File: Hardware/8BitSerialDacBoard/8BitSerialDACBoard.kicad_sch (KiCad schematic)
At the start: 28 parts, among them J1 Conn_01x08, U1 SN74LV595APWRG4

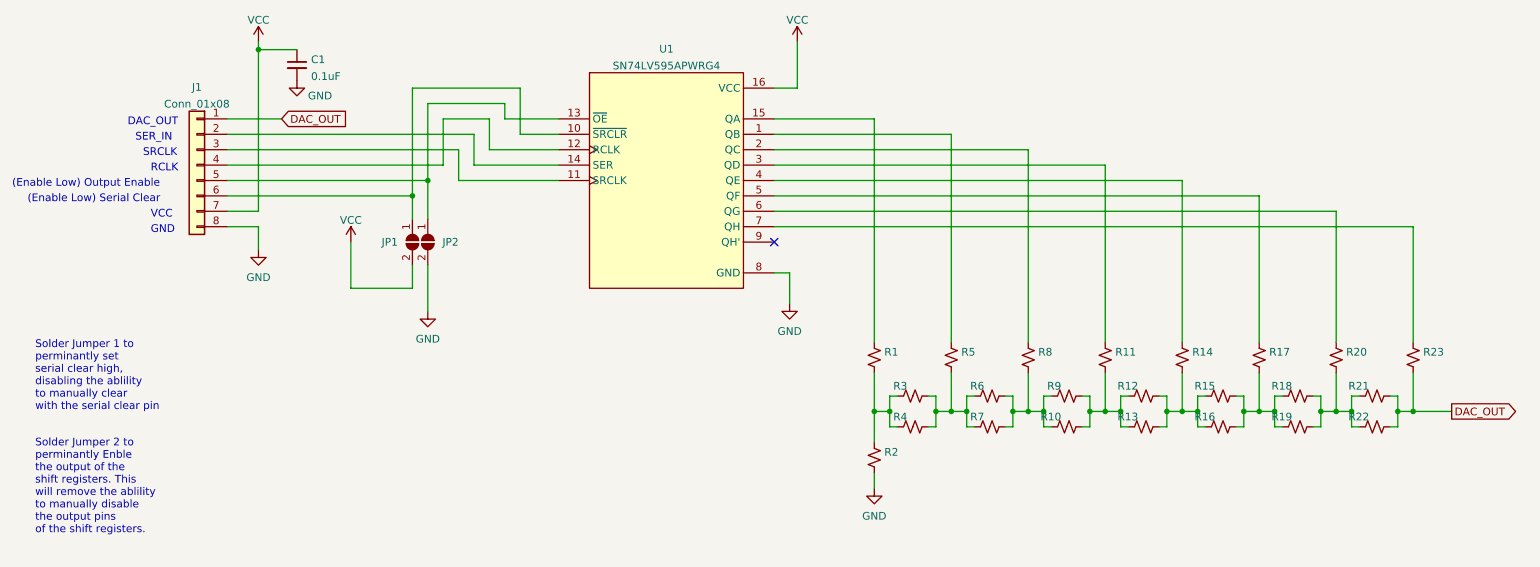
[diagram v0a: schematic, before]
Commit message: Adding chainablity to DACs, need to flip bit direction
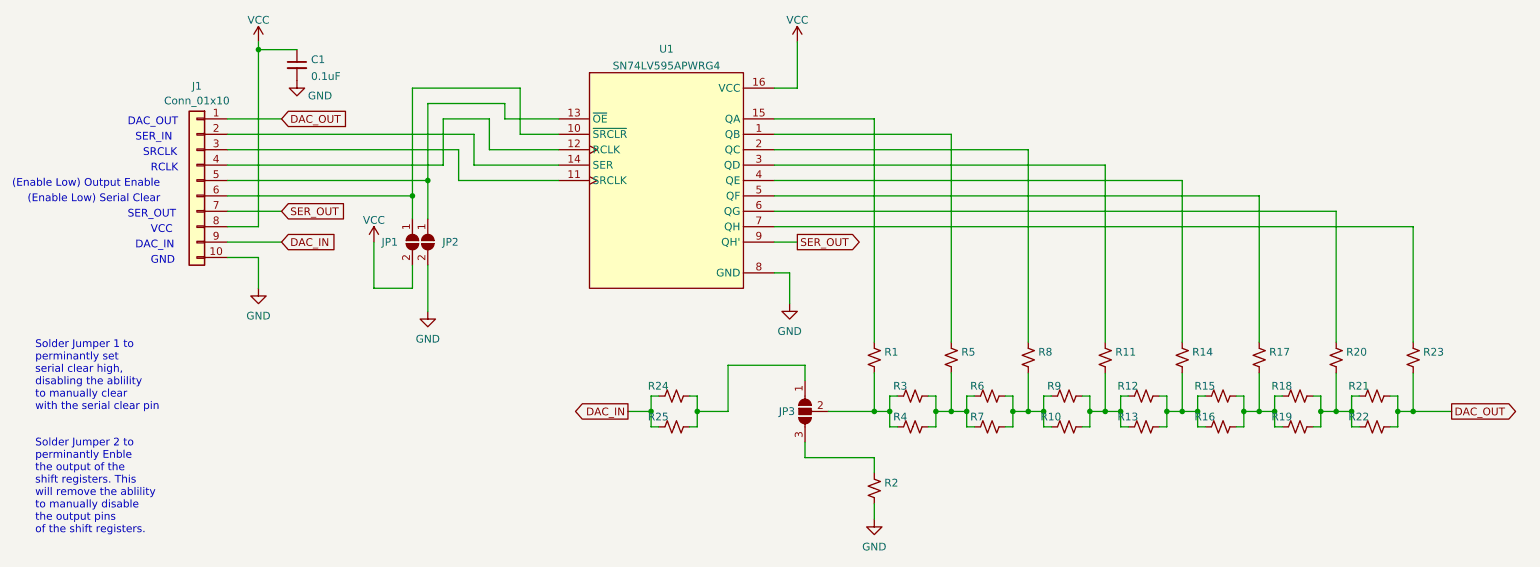
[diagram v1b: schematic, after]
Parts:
- removed J1: Conn_01x08, Connector_PinHeader_2.54mm:PinHeader_1x08_P2.54mm_Vertical, symbol Connector_Generic:Conn_01x08
- added J1: Conn_01x10, Connector_PinHeader_2.54mm:PinHeader_1x10_P2.54mm_Vertical, symbol Connector_Generic:Conn_01x10
- added JP3: SolderJumper_3_Open, Jumper:SolderJumper-3_P1.3mm_Open_RoundedPad1.0x1.5mm, symbol Jumper:SolderJumper_3_Open
- added R24, R25: R_Small_US, Resistor_SMD:R_0603_1608Metric_Pad0.98x0.95mm_HandSolder, symbol Device:R_Small_US
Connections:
- net DAC_OUT: now also J1.1 (Pin_1)
- net GND: now also J1.10 (Pin_10)
- net VCC: now also J1.8 (Pin_8)
- net at R1.2, R3.1, R4.1: now also JP3.2 (C); no longer R2.1
- net at JP2.1 (A), U1.13 (~{OE}): now also J1.5 (Pin_5)
- net at JP1.1 (A), U1.10 (~{SRCLR}): now also J1.6 (Pin_6)
- net at U1.11 (SRCLK): now also J1.3 (Pin_3)
- net at U1.12 (RCLK): now also J1.4 (Pin_4)
- net at U1.14 (SER): now also J1.2 (Pin_2)
- net SER_OUT: now reaches U1.9 (QH')
- net SER_OUT: now also J1.7 (Pin_7)
- new net: JP3.3 (B), R2.1
- new net: JP3.1 (A), R24.2, R25.2
- new net DAC_IN: J1.9 (Pin_9), R24.1, R25.1
- no-connect marks 1 -> 0
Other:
- note added: "DAC_IN"
- note added: "SER_OUT"
- moved on the sheet: R2
